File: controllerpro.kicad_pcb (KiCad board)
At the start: 2 copper layers, 92.7 x 50.8 mm, 19 parts, among them P0 Conn_01x08_Male, P2 Conn_01x08_Male, U1 Teensy3.2

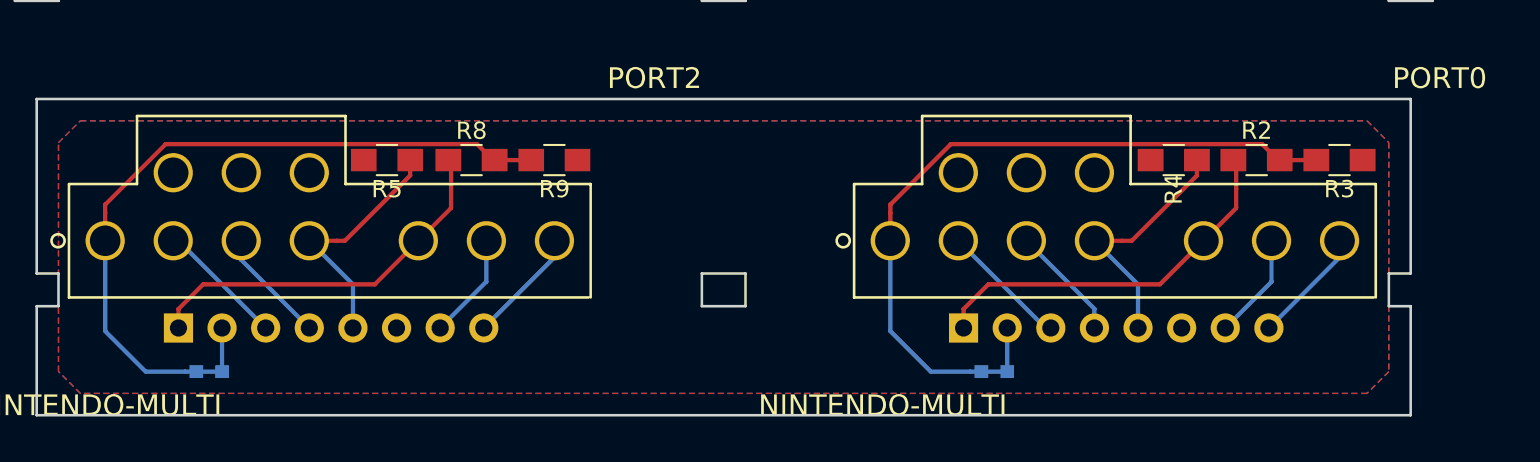
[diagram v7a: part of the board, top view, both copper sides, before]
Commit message: Switch to solder bridges for the SNES mode selectors
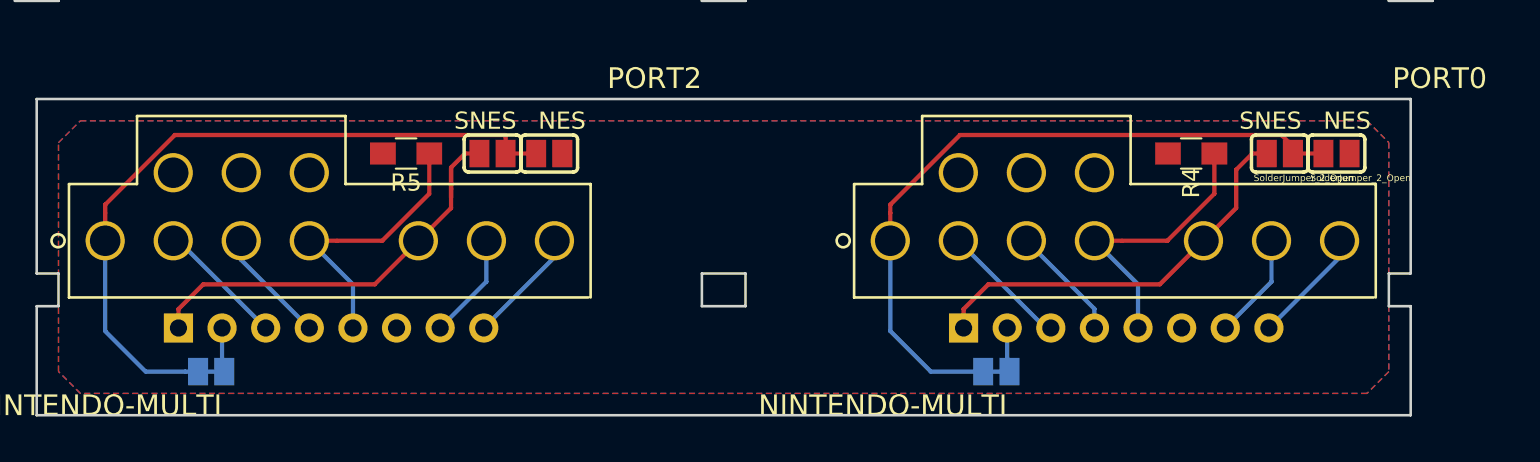
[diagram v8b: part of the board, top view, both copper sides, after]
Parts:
- removed R1, R7: R, Capacitors_SMD:C_0603
- removed R2, R3, R8, R9: R, Resistors_SMD:R_0805_HandSoldering
- added JP2: SolderJumper_2_Bridged, t32_ref:SOLDERJUMPER, B.Cu at (163.8, 140.3)
- added JP3: SolderJumper_2_Open, t32_ref:SOLDERJUMPER, F.Cu at (180.3, 127.6)
- added JP4: SolderJumper_2_Open, t32_ref:SOLDERJUMPER, F.Cu at (183.6, 127.6)
- added JP5: SolderJumper_2_Bridged, t32_ref:SOLDERJUMPER, B.Cu at (118.1, 140.3)
- added JP6: SolderJumper_2_Open, t32_ref:SOLDERJUMPER, F.Cu at (134.5, 127.6)
- added JP7: SolderJumper_2_Open, t32_ref:SOLDERJUMPER, F.Cu at (137.8, 127.6)
- moved R5 1.17 mm to (129.5, 127.6)
- moved R4 1.09 mm to (175.2, 127.6)
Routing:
- net VCCA: track 43.4 -> 49.2 mm
- net Net-(P2-Pad5): track 14.5 -> 16.6 mm
- net Net-(P0-Pad5): track 14.6 -> 16.6 mm
- net Net-(JP5-Pad1): track 44.3 -> 45.5 mm
- net Net-(JP2-Pad1): track 44.3 -> 45.5 mm
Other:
- board text added: "NES"
- board text added: "SNES"
- board text added: "SNES+NES"
